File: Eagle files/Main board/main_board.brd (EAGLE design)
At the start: 64 x 90 mm, 63 parts, among them X1 ARK2, X2 ARK1

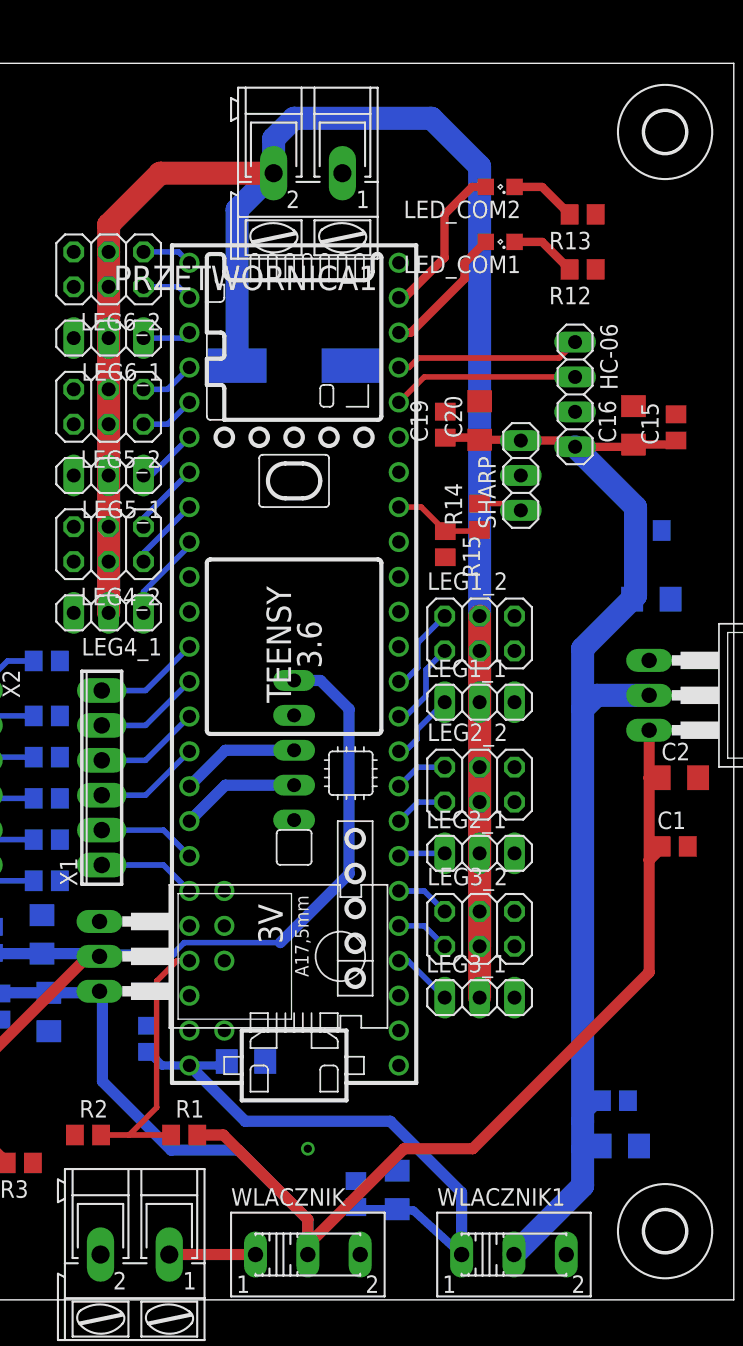
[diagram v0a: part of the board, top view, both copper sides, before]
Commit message: update pcb
-increase servo power line width
-added step-down regulator enable
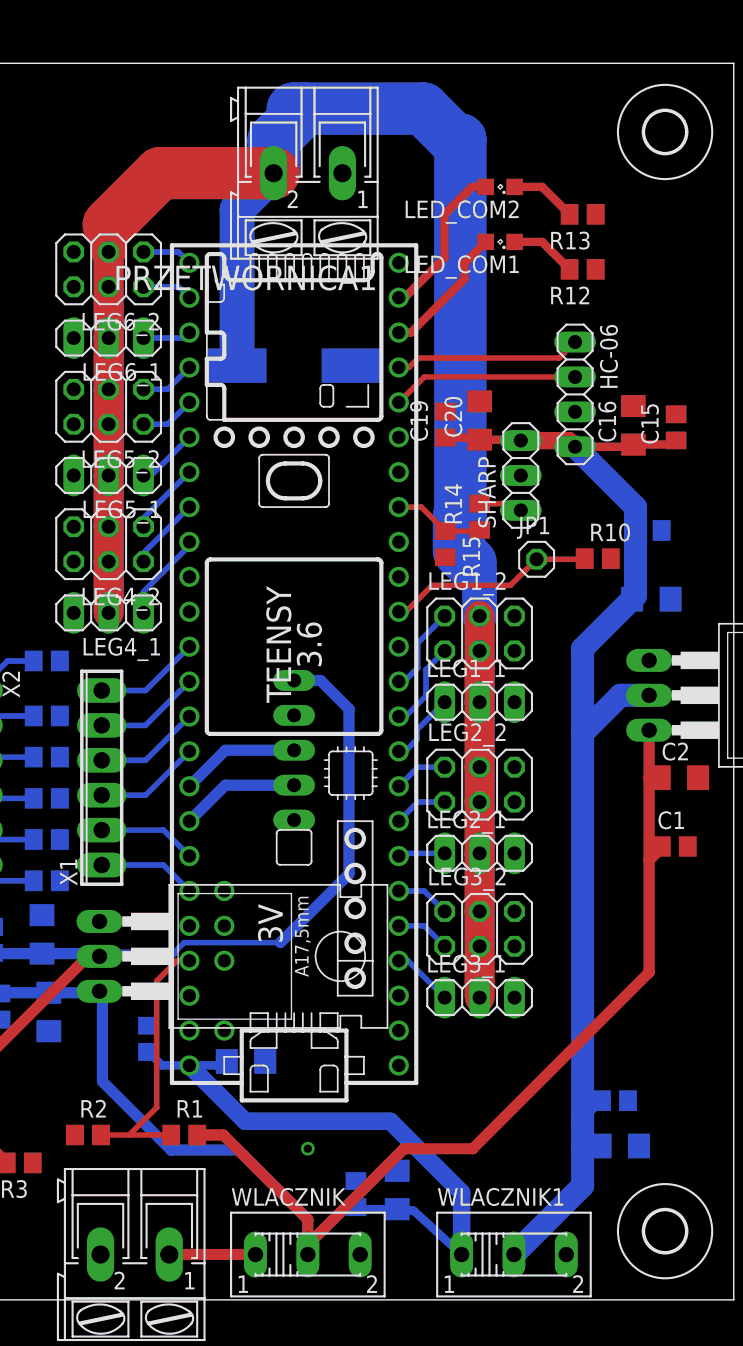
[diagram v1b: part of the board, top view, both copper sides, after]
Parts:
- added JP1: (no value), pinhead:1X01
- added R10: 100k, rcl:R0805
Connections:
- removed net BATTERY2: TEENSY41.22/A8
- removed net LED(BOARD): TEENSY41.13/SCK
- new net EN_PRZETWOTNICA: JP1.1, R10.1, TEENSY41.12/MISO
- net GND: now also R10.2
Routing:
- net EN_PRZETWOTNICA: track 0.00 -> 15.1 mm
- net +6V: track 182.2 -> 184.9 mm
- net +5V: track 90.3 -> 91.0 mm
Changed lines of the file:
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@@
 <element name="C19" library="rcl" package="C0805" value="100n" x="11" y="18.7" rot="R90"/>
 <element name="C20" library="rcl" package="C1206" value="10uF" x="13.5" y="19" rot="R90"/>
+<element name="JP1" library="pinhead" package="1X01" value="" x="17.65" y="8.9"/>
+<element name="R10" library="rcl" package="R0805" value="100k" x="22.1" y="8.95"/>
 </elements>
 <signals>
@@
 <contactref element="C20" pad="2"/>
 <via x="1" y="-34" extent="1-16" drill="0.6" shape="square"/>
+<contactref element="R10" pad="2"/>
 </signal>
 <signal name="PWM1_1">
@@
 <wire x1="13.5" y1="17.6" x2="16.44" y2="17.6" width="0.6096" layer="1"/>
 <wire x1="16.44" y1="17.6" x2="16.5" y2="17.54" width="0.6096" layer="1"/>
-<wire x1="16.5" y1="17.54" x2="20" y2="17.54" width="0.6096" layer="1"/>
-<wire x1="20" y1="17.54" x2="20.45" y2="17.09" width="0.6096" layer="1"/>
+<wire x1="16.5" y1="17.54" x2="20" y2="17.54" width="1.27" layer="1"/>
+<wire x1="20" y1="17.54" x2="20.45" y2="17.09" width="1.27" layer="1"/>
 <wire x1="20.45" y1="17.09" x2="24.54" y2="17.09" width="0.6096" layer="1"/>
 <wire x1="24.54" y1="17.09" x2="24.7" y2="17.25" width="0.6096" layer="1"/>
 <wire x1="24.7" y1="17.25" x2="27.5" y2="17.25" width="0.6096" layer="1"/>
 <wire x1="27.5" y1="17.25" x2="27.8" y2="17.55" width="0.6096" layer="1"/>
-<wire x1="25.84" y1="-1" x2="22" y2="-1" width="1.6764" layer="16"/>
-<wire x1="22" y1="-1" x2="21" y2="-2" width="1.6764" layer="16"/>
-<wire x1="21" y1="-2" x2="21" y2="-32" width="1.6764" layer="16"/>
+<wire x1="21" y1="2.4" x2="21" y2="-3.75" width="1.6764" layer="16"/>
+<wire x1="21" y1="-3.75" x2="21" y2="-32" width="1.6764" layer="16"/>
 <wire x1="21" y1="-32" x2="21" y2="-34" width="1.6764" layer="16"/>
 <wire x1="21" y1="-34" x2="21" y2="-36.7" width="1.6764" layer="16"/>
 <wire x1="21" y1="-36.7" x2="16" y2="-41.7" width="1.6764" layer="16"/>
 <wire x1="24.6" y1="6" x2="21" y2="2.4" width="1.6764" layer="16"/>
-<wire x1="21" y1="2.4" x2="21" y2="-2" width="1.6764" layer="16"/>
 <wire x1="24.6" y1="6" x2="24.85" y2="6.25" width="1.6764" layer="16"/>
 <wire x1="24.85" y1="6.25" x2="24.85" y2="11" width="1.6764" layer="16"/>
@@
 <wire x1="22.3" y1="-33.8" x2="21.2" y2="-33.8" width="0.4064" layer="16"/>
 <wire x1="21.2" y1="-33.8" x2="21" y2="-34" width="0.4064" layer="16"/>
+<wire x1="25.84" y1="-1" x2="23.75" y2="-1" width="1.6764" layer="16"/>
+<wire x1="23.75" y1="-1" x2="21" y2="-3.75" width="1.6764" layer="16"/>
 </signal>
 <signal name="LEG6">
@@
 <wire x1="9.47" y1="22.17" x2="7.62" y2="20.32" width="0.4064" layer="1"/>
 </signal>
-<signal name="LED(BOARD)">
-<contactref element="TEENSY41" pad="13/SCK"/>
-</signal>
 <signal name="N$1">
 <contactref element="R4" pad="2"/>
@@
 <contactref element="BATERIA" pad="1"/>
 <wire x1="-9.0854" y1="-41.7" x2="-2.81" y2="-41.7" width="0.8128" layer="1"/>
-</signal>
-<signal name="BATTERY2">
-<contactref element="TEENSY41" pad="22/A8"/>
 </signal>
 <signal name="N$8">
@@
 <contactref element="TEENSY41" pad="VIN"/>
 <contactref element="WLACZNIK1" pad="1"/>
-<wire x1="12.19" y1="-41.7" x2="12.19" y2="-37.19" width="0.8128" layer="16"/>
-<wire x1="12.19" y1="-37.19" x2="7" y2="-32" width="0.8128" layer="16"/>
-<wire x1="7" y1="-32" x2="-3.56" y2="-32" width="0.8128" layer="16"/>
-<wire x1="-3.56" y1="-32" x2="-7.62" y2="-27.94" width="0.8128" layer="16"/>
+<wire x1="12.19" y1="-41.7" x2="12.19" y2="-37.19" width="1.27" layer="16"/>
+<wire x1="12.19" y1="-37.19" x2="7" y2="-32" width="1.27" layer="16"/>
+<wire x1="7" y1="-32" x2="-3.56" y2="-32" width="1.27" layer="16"/>
+<wire x1="-3.56" y1="-32" x2="-7.62" y2="-27.94" width="1.27" layer="16"/>
 <contactref element="C12" pad="1"/>
 <contactref element="C11" pad="1"/>
@@
 <contactref element="LEG2_1" pad="2"/>
 <contactref element="LEG3_2" pad="4"/>
-<wire x1="13.5" y1="-16.73" x2="13.5" y2="-12.5" width="1.6764" layer="16"/>
+<wire x1="13.5" y1="-16.73" x2="13.5" y2="-12.5" width="2.1844" layer="16"/>
 <contactref element="LEG4_1" pad="2"/>
 <contactref element="LEG4_2" pad="3"/>
@@
 <contactref element="LEG6_2" pad="4"/>
 <contactref element="LEG6_1" pad="2"/>
-<wire x1="-13.5" y1="25" x2="-13.5" y2="21.27" width="1.6764" layer="16"/>
-<wire x1="-13.5" y1="21.27" x2="-13.5" y2="18.73" width="1.6764" layer="16"/>
-<wire x1="-13.5" y1="18.73" x2="-13.5" y2="15" width="1.6764" layer="16"/>
-<wire x1="-13.5" y1="8.73" x2="-13.5" y2="11.27" width="1.6764" layer="16"/>
-<wire x1="-13.5" y1="11.27" x2="-13.5" y2="15" width="1.6764" layer="16"/>
-<wire x1="-13.5" y1="25" x2="-13.5" y2="28.73" width="1.6764" layer="16"/>
-<wire x1="-13.5" y1="31.27" x2="-13.5" y2="5" width="1.6764" layer="1"/>
-<wire x1="13.5" y1="2.23" x2="13.5" y2="-1.5" width="1.6764" layer="16"/>
-<wire x1="13.5" y1="-1.5" x2="13.5" y2="-6.23" width="1.6764" layer="16"/>
-<wire x1="13.5" y1="-6.23" x2="13.5" y2="-8.77" width="1.6764" layer="16"/>
-<wire x1="13.5" y1="-8.77" x2="13.5" y2="-12.5" width="1.6764" layer="16"/>
-<wire x1="13.5" y1="-16.73" x2="13.5" y2="-19.27" width="1.6764" layer="16"/>
-<wire x1="13.5" y1="-23" x2="13.5" y2="4.77" width="1.6764" layer="1"/>
-<wire x1="-1.4892" y1="37" x2="-9.75" y2="37" width="1.6764" layer="1"/>
-<wire x1="-13.5" y1="5" x2="-13.5" y2="8.73" width="1.6764" layer="16"/>
-<wire x1="13.5" y1="4.77" x2="13.5" y2="37.5" width="1.6764" layer="16"/>
-<wire x1="-4.15" y1="23" x2="-4.15" y2="34.3392" width="1.6764" layer="16"/>
-<wire x1="-4.15" y1="34.3392" x2="-1.4892" y2="37" width="1.6764" layer="16"/>
-<wire x1="-13.5" y1="31.27" x2="-13.5" y2="33.25" width="1.6764" layer="1"/>
-<wire x1="-9.75" y1="37" x2="-13.5" y2="33.25" width="1.6764" layer="1"/>
-<wire x1="-1.4892" y1="37" x2="-1.4892" y2="39.5108" width="1.6764" layer="16"/>
-<wire x1="-1.4892" y1="39.5108" x2="0" y2="41" width="1.6764" layer="16"/>
-<wire x1="13.5" y1="37.5" x2="10" y2="41" width="1.6764" layer="16"/>
-<wire x1="10" y1="41" x2="0" y2="41" width="1.6764" layer="16"/>
+<wire x1="-13.5" y1="25" x2="-13.5" y2="21.27" width="2.1844" layer="16"/>
+<wire x1="-13.5" y1="21.27" x2="-13.5" y2="18.73" width="2.1844" layer="16"/>
+<wire x1="-13.5" y1="18.73" x2="-13.5" y2="15" width="2.1844" layer="16"/>
+<wire x1="-13.5" y1="8.73" x2="-13.5" y2="11.27" width="2.1844" layer="16"/>
+<wire x1="-13.5" y1="11.27" x2="-13.5" y2="15" width="2.1844" layer="16"/>
+<wire x1="-13.5" y1="25" x2="-13.5" y2="28.73" width="2.1844" layer="16"/>
+<wire x1="-13.5" y1="31.27" x2="-13.5" y2="5" width="2.1844" layer="1"/>
+<wire x1="13.5" y1="2.23" x2="13.5" y2="-1.5" width="2.1844" layer="16"/>
+<wire x1="13.5" y1="-1.5" x2="13.5" y2="-6.23" width="2.1844" layer="16"/>
+<wire x1="13.5" y1="-6.23" x2="13.5" y2="-8.77" width="2.1844" layer="16"/>
+<wire x1="13.5" y1="-8.77" x2="13.5" y2="-12.5" width="2.1844" layer="16"/>
+<wire x1="13.5" y1="-16.73" x2="13.5" y2="-19.27" width="2.1844" layer="16"/>
+<wire x1="13.5" y1="-23" x2="13.5" y2="4.77" width="2.1844" layer="1"/>
+<wire x1="-1.4892" y1="37" x2="-9.75" y2="37" width="3.81" layer="1"/>
+<wire x1="-13.5" y1="5" x2="-13.5" y2="8.73" width="2.1844" layer="16"/>
+<wire x1="-4.15" y1="23" x2="-4.15" y2="34.3392" width="2.54" layer="16"/>
+<wire x1="-4.15" y1="34.3392" x2="-1.4892" y2="37" width="2.54" layer="16"/>
+<wire x1="-13.5" y1="31.27" x2="-13.5" y2="33.25" width="2.54" layer="1"/>
+<wire x1="-9.75" y1="37" x2="-13.5" y2="33.25" width="3.81" layer="1"/>
+<wire x1="12.1" y1="39.45" x2="12.1" y2="12.1" width="3.81" layer="16"/>
+<wire x1="12.1" y1="12.1" x2="12" y2="12" width="3.81" layer="16"/>
+<wire x1="12" y1="12" x2="12" y2="9.5" width="3.81" layer="16"/>
+<wire x1="12" y1="9.5" x2="12.25" y2="9.25" width="3.81" layer="16"/>
+<wire x1="12.25" y1="9.25" x2="12.85" y2="8.65" width="3.81" layer="16"/>
+<wire x1="13.5" y1="4.77" x2="13.5" y2="8" width="2.54" layer="16"/>
+<wire x1="13.5" y1="8" x2="12.25" y2="9.25" width="2.54" layer="16"/>
+<wire x1="12.1" y1="39.45" x2="11.65" y2="39.45" width="3.81" layer="16"/>
+<wire x1="11.65" y1="39.45" x2="9.4" y2="41.7" width="3.81" layer="16"/>
+<wire x1="9.4" y1="41.7" x2="0.8" y2="41.7" width="3.81" layer="16"/>
+<wire x1="0.8" y1="41.7" x2="-0.05" y2="41.7" width="3.81" layer="16"/>
+<wire x1="-0.05" y1="41.7" x2="-0.1" y2="41.65" width="3.81" layer="16"/>
+<wire x1="-1.4892" y1="37" x2="-1.4892" y2="39.4108" width="3.81" layer="16"/>
+<wire x1="-1.4892" y1="39.4108" x2="0.8" y2="41.7" width="3.81" layer="16"/>
 <wire x1="13.5" y1="4.77" x2="13.5" y2="2.23" width="0" layer="19" extent="1-1"/>
 </signal>
+<signal name="EN_PRZETWOTNICA">
+<contactref element="TEENSY41" pad="12/MISO"/>
+<contactref element="JP1" pad="1"/>
+<wire x1="7.62" y1="5.08" x2="8.13" y2="5.08" width="0.4064" layer="1"/>
+<wire x1="8.13" y1="5.08" x2="10.05" y2="7" width="0.4064" layer="1"/>
+<wire x1="10.05" y1="7" x2="15.75" y2="7" width="0.4064" layer="1"/>
+<wire x1="15.75" y1="7" x2="17.65" y2="8.9" width="0.4064" layer="1"/>
+<contactref element="R10" pad="1"/>
+<wire x1="21.15" y1="8.95" x2="21.1" y2="8.9" width="0.4064" layer="1"/>
+<wire x1="21.1" y1="8.9" x2="17.65" y2="8.9" width="0.4064" layer="1"/>
+</signal>
 </signals>

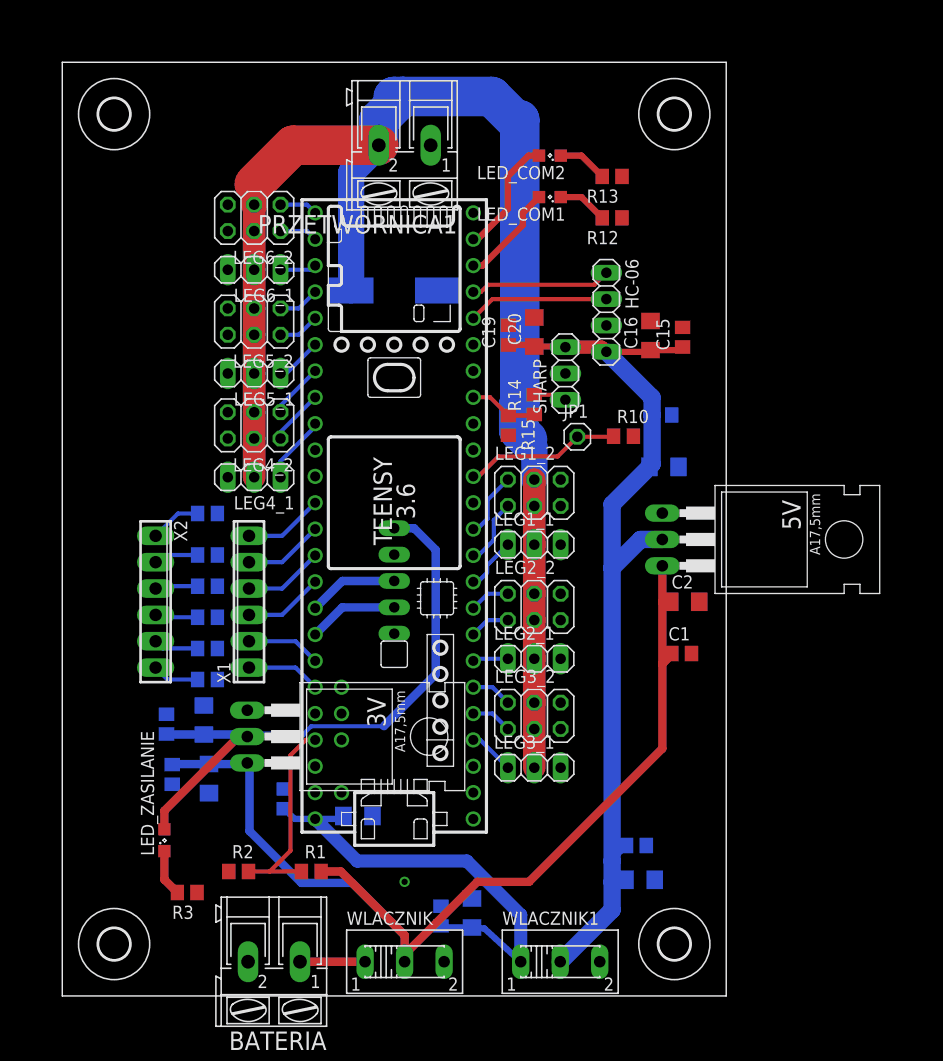
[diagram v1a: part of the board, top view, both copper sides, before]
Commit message: Update main_board.brd
Deacrease board size
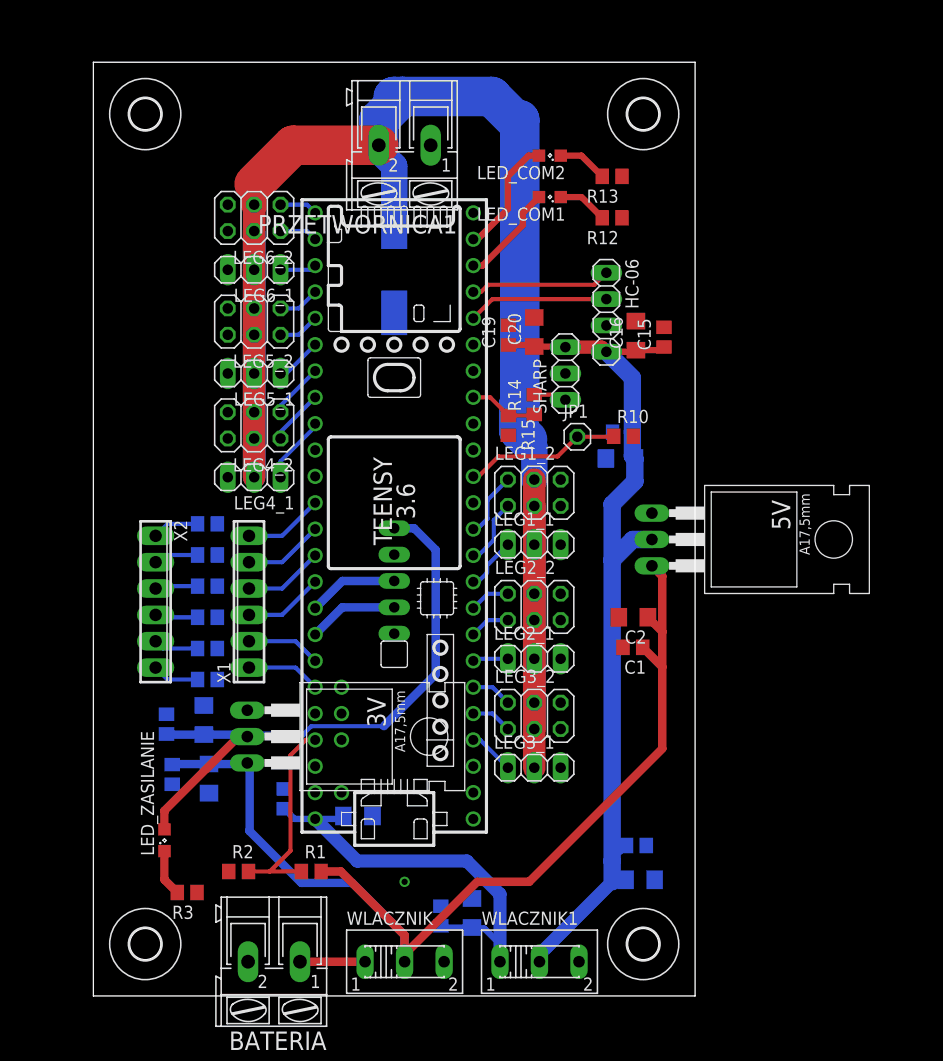
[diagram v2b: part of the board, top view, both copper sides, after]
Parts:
- moved C2 5.17 mm to (23.1, -8.50), turned to 180 degrees
- moved C1 4.74 mm to (23.0, -11.4), turned to 180 degrees
- moved C3 4.28 mm to (21.8, 6.80), turned to 0 degrees
- moved C4 4.14 mm to (22.0, 9.35), turned to 0 degrees
- moved H1 3.00 mm to (24.0, 40.0)
- moved H2 3.00 mm to (-24.0, 40.0)
- moved H3 3.00 mm to (24.0, -40.0)
- moved H4 3.00 mm to (-24.0, -40.0)
- moved C5 2.00 mm to (0.00, 25.0), turned to 90 degrees
- moved WLACZNIK1 2.00 mm to (14.0, -41.7)
- moved C15 1.80 mm to (26.0, 18.5)
- moved C16 1.40 mm to (23.3, 18.6)
- moved 5V 1.00 mm to (35.0, -1.00)
- moved R9 1.00 mm to (-18.0, 0.50)
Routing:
- net +6V: track 184.9 -> 181.1 mm
- net +5V: track 91.0 -> 87.6 mm
- net +BAT: track 102.3 -> 105.2 mm
- net +5MCU: track 43.4 -> 41.6 mm
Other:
- board size 64 x 90 mm -> 58 x 90 mm
